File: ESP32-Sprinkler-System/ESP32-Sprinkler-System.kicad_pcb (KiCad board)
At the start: 2 copper layers, 207 x 158.8 mm, 58 parts, among them J101 12V, J102 DHT, J103 NEOPIXEL, J104 LCD, J105 BME280, J201 TBL004-508-02BE-2GY, J202 TBL004-508-02BE-2GY, J203 TBL004-508-02BE-2GY, J204 TBL004-508-02BE-2GY, Q201 IRFZ24NPBF, Q202 IRFZ24NPBF, Q203 IRFZ24NPBF, Q204 IRFZ24NPBF, U101 V7805-500, U102 ESP32-DEVKITC-32D, U201 MC33152PG, U202 MC33152PG

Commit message: Traces complete
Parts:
- moved S101 1.42 mm to (180.3, 120.7)
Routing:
- net 3.3V: track 0.00 -> 95.0 mm, vias 0 -> 2
- net SW_A: track 0.00 -> 73.2 mm
- net DHT: track 0.00 -> 65.7 mm, vias 0 -> 2
- net MOSI: track 0.00 -> 49.3 mm
- net SCK: track 0.00 -> 45.3 mm
- net D/C: track 0.00 -> 34.0 mm
- net 5V: track 30.7 -> 64.2 mm
- net BACKLIGHT: track 0.00 -> 26.3 mm
- net SDA: track 0.00 -> 24.9 mm
- net CS: track 0.00 -> 21.2 mm
- net 12V: track 241.9 -> 262.9 mm
- net SCL: track 0.00 -> 17.7 mm
- net NEOPIXEL: track 0.00 -> 16.7 mm
- net Valve1: track 0.00 -> 13.3 mm
- net Valve4: track 0.00 -> 9.91 mm
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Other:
- board size 207 x 158.8 mm -> 134.6 x 73.7 mm

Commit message: curvy 2 saved
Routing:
- net 12V: track 262.9 -> 257.8 mm
- net D/C: track 34.0 -> 33.0 mm
- net MOSI: track 49.3 -> 48.4 mm
- net SW_A: track 73.2 -> 72.3 mm
- net 3.3V: track 95.0 -> 94.2 mm
- net Net-(R218-Pad1): track 35.9 -> 35.1 mm
- net SCK: track 45.3 -> 44.6 mm
- net 5V: track 64.2 -> 63.5 mm
- net DHT: track 65.7 -> 65.1 mm
- net Net-(D206-Pad2): track 25.9 -> 25.3 mm
- net Net-(R202-Pad1): track 25.0 -> 24.4 mm

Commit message: added some labels and stuff
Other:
- board text added: "+12"
- board text added: "3.3V CS SCK MOSI DC BL GND"
- board text added: "3.3V GND SCL SDA"
- board text added: "3.3V IO5 GND"
- board text added: "5V IO2 GND"
- board text added: "GND"
- board text added: "IO23"
- board text added: "Power In"
- board text added: "Zone1:IO32"
- board text added: "Zone2:IO33"
- board text added: "Zone3:IO25"
- board text added: "Zone4:IO26"
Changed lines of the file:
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@@
     (property "Sheetname" "")
     (attr through_hole)
-    (fp_text reference "J105" (at 2.515 -0.02 180) (layer "F.SilkS")
-      (effects (font (size 1 1) (thickness 0.15)))
-    )
-    (fp_text value "BME280" (at 2.605 8.01 180) (layer "F.SilkS")
+    (fp_text reference "J105" (at 2.515 -0.02 180) (layer "F.SilkS") hide
+      (effects (font (size 1 1) (thickness 0.15)))
+    )
+    (fp_text value "BME280" (at 7.685 8.01 180) (layer "F.SilkS")
       (effects (font (size 1 1) (thickness 0.15)))
     )
@@
     (property "Sheetname" "")
     (attr exclude_from_pos_files)
-    (fp_text reference "S101" (at 0 -6.604) (layer "F.SilkS")
+    (fp_text reference "S101" (at 0 0) (layer "F.SilkS")
       (effects (font (size 0.6096 0.6096) (thickness 0.127)))
     )
@@
     (property "Sheetname" "")
     (attr through_hole)
-    (fp_text reference "J104" (at 2.3107 0.014 180) (layer "F.SilkS")
-      (effects (font (size 1 1) (thickness 0.15)))
-    )
-    (fp_text value "LCD" (at 2.4007 8.044 180) (layer "F.SilkS")
+    (fp_text reference "J104" (at 2.3107 0.014 180) (layer "F.SilkS") hide
+      (effects (font (size 1 1) (thickness 0.15)))
+    )
+    (fp_text value "LCD" (at 11.9257 7.409 180) (layer "F.SilkS")
       (effects (font (size 1 1) (thickness 0.15)))
     )
@@
     (property "Sheetname" "")
     (attr through_hole)
-    (fp_text reference "J102" (at 2.54 0 180) (layer "F.SilkS")
-      (effects (font (size 1 1) (thickness 0.15)))
-    )
-    (fp_text value "DHT" (at 2.63 4.22 180) (layer "F.SilkS")
+    (fp_text reference "J102" (at 2.54 0 180) (layer "F.SilkS") hide
+      (effects (font (size 1 1) (thickness 0.15)))
+    )
+    (fp_text value "DHT" (at -2.45 4.22 180) (layer "F.SilkS")
       (effects (font (size 1 1) (thickness 0.15)))
     )
@@
     (property "Sheetname" "")
     (attr through_hole)
-    (fp_text reference "U102" (at -10.829175 -24.765) (layer "F.SilkS")
+    (fp_text reference "U102" (at -10.829175 -24.765) (layer "F.SilkS") hide
       (effects (font (size 1.000386 1.000386) (thickness 0.15)))
     )
@@
     (property "Sheetname" "")
     (attr through_hole)
-    (fp_text reference "C105" (at 6.35 0 180) (layer "F.SilkS")
+    (fp_text reference "C105" (at 5.805 0 180) (layer "F.SilkS")
       (effects (font (size 1 1) (thickness 0.15)))
     )
@@
     (property "Sheetname" "")
     (attr through_hole)
-    (fp_text reference "J103" (at 2.54 0 180) (layer "F.SilkS")
-      (effects (font (size 1 1) (thickness 0.15)))
-    )
-    (fp_text value "NEOPIXEL" (at -2.45 2.54 180) (layer "F.SilkS")
+    (fp_text reference "J103" (at 2.54 0 180) (layer "F.SilkS") hide
+      (effects (font (size 1 1) (thickness 0.15)))
+    )
+    (fp_text value "NEOPIXEL" (at 7.075 2.54 180) (layer "F.SilkS")
       (effects (font (size 1 1) (thickness 0.15)))
     )
@@
   (gr_rect (start 355.28 125.1) (end 300.78 55.1) (layer "Dwgs.User") (width 0.15) (fill none))
   (gr_rect (start 58.01 61.05) (end 192.63 134.71) (layer "Edge.Cuts") (width 0.1) (fill none))
+  (gr_text "Power In" (at 109.22 133.985) (layer "F.SilkS")
+    (effects (font (size 1 1) (thickness 0.15)))
+  )
+  (gr_text "+12" (at 100.33 132.08) (layer "F.SilkS")
+    (effects (font (size 1 1) (thickness 0.15)))
+  )
+  (gr_text "+12" (at 60.96 97.79) (layer "F.SilkS")
+    (effects (font (size 1 1) (thickness 0.15)))
+  )
+  (gr_text "+12" (at 60.96 115.57) (layer "F.SilkS")
+    (effects (font (size 1 1) (thickness 0.15)))
+  )
+  (gr_text "GND" (at 116.84 132.08) (layer "F.SilkS")
+    (effects (font (size 1 1) (thickness 0.15)))
+  )
+  (gr_text "Zone2:IO33" (at 66.04 95.25) (layer "F.SilkS")
+    (effects (font (size 1 1) (thickness 0.15)))
+  )
+  (gr_text "3.3V\n\nGND\nSCL\n\nSDA" (at 172.308348 82.021383 90) (layer "F.SilkS")
+    (effects (font (size 1.5 1) (thickness 0.15)) (justify left))
+  )
+  (gr_text "Zone3:IO25" (at 66.04 113.03) (layer "F.SilkS")
+    (effects (font (size 1 1) (thickness 0.15)))
+  )
+  (gr_text "3.3V\nIO5\n\nGND" (at 107.315 67.945 90) (layer "F.SilkS")
+    (effects (font (size 1.5 1) (thickness 0.15)) (justify left))
+  )
+  (gr_text "IO23" (at 180.34 118.11) (layer "F.SilkS")
+    (effects (font (size 1 1) (thickness 0.15)))
+  )
+  (gr_text "+12" (at 60.96 80.01) (layer "F.SilkS")
+    (effects (font (size 1 1) (thickness 0.15)))
+  )
+  (gr_text "+12" (at 60.96 62.23) (layer "F.SilkS")
+    (effects (font (size 1 1) (thickness 0.15)))
+  )
+  (gr_text "3.3V\nCS\nSCK\nMOSI\nDC\nBL\nGND" (at 174.74745 107.95 90) (layer "F.SilkS")
+    (effects (font (size 1.5 1) (thickness 0.15)) (justify left))
+  )
+  (gr_text "Zone4:IO26" (at 66.04 130.81) (layer "F.SilkS")
+    (effects (font (size 1 1) (thickness 0.15)))
+  )
+  (gr_text "5V\nIO2\nGND" (at 166.034612 123.19 90) (layer "F.SilkS")
+    (effects (font (size 1.5 1) (thickness 0.15)) (justify left))
+  )
+  (gr_text "Zone1:IO32" (at 66.04 77.47) (layer "F.SilkS")
+    (effects (font (size 1 1) (thickness 0.15)))
+  )
   (dimension (type aligned) (layer "Dwgs.User")
     (pts (xy 355.28 36.6) (xy 300.78 36.6))

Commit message: TIDY UP AND ANOTATE
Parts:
- added REF**: Breadstick B Silk 5mm, _Breadstick_Footprints:Breadstick B Silk 5mm, F.Cu at (188.0, 130.8)
- added REF**: Breadstick B 10mm v2, _Breadstick_Footprints:Breadstick B 10mm v2, F.Cu at (174.6, 93.3)
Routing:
- net 3.3V: track 94.2 -> 108.3 mm, vias 2 -> 0
- net GND: track 7.83 -> 0.00 mm, vias 4 -> 0
- net D/C: track 33.0 -> 26.4 mm
- net CS: track 20.8 -> 22.9 mm
- net BACKLIGHT: track 25.9 -> 27.7 mm
- net 12V: track 257.8 -> 259.4 mm
- net Net-(R202-Pad1): track 24.4 -> 25.9 mm
- net MOSI: track 48.4 -> 49.7 mm
- net SCK: track 44.6 -> 45.3 mm
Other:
- board text added: "J & R Creative Technologies Inc."
- board text added: "https://github.com/mrangen/ESP32-Sprinkler-System"

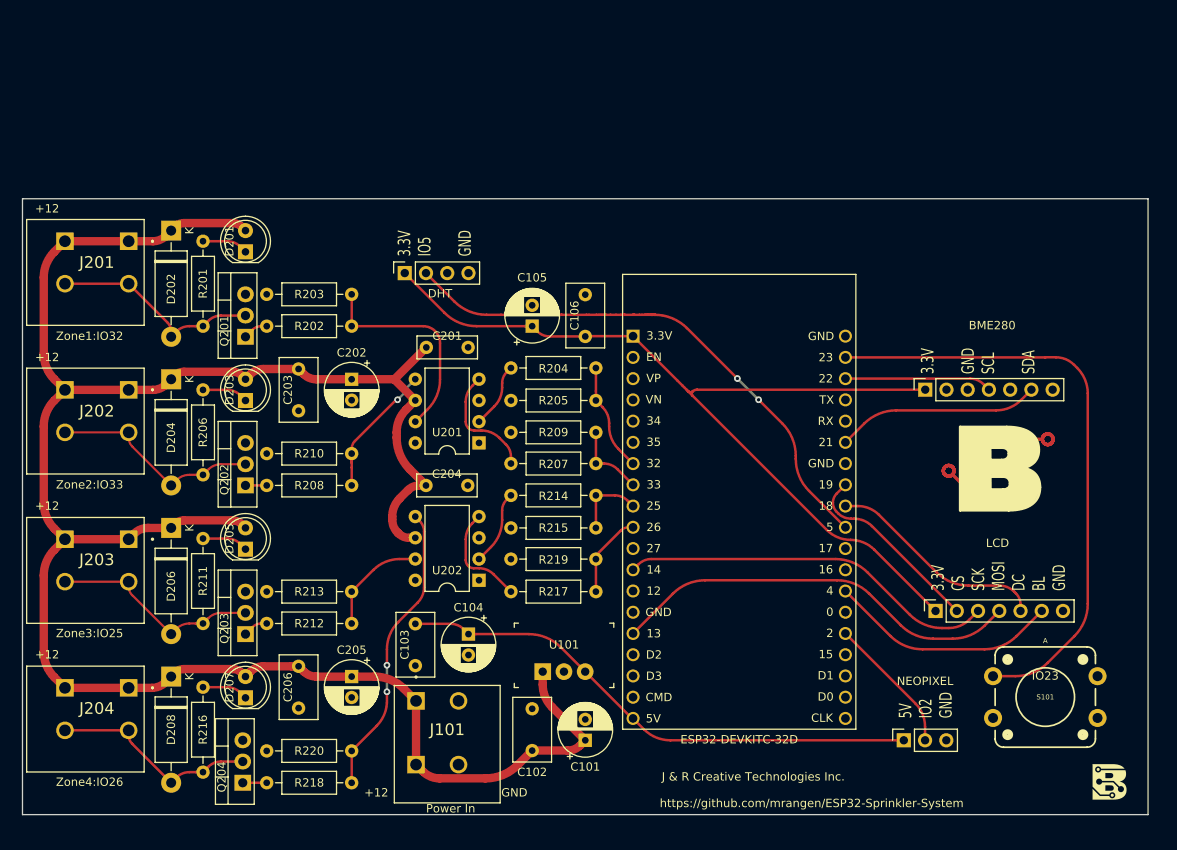
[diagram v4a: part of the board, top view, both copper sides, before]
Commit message: Added M3 Mounting Holes
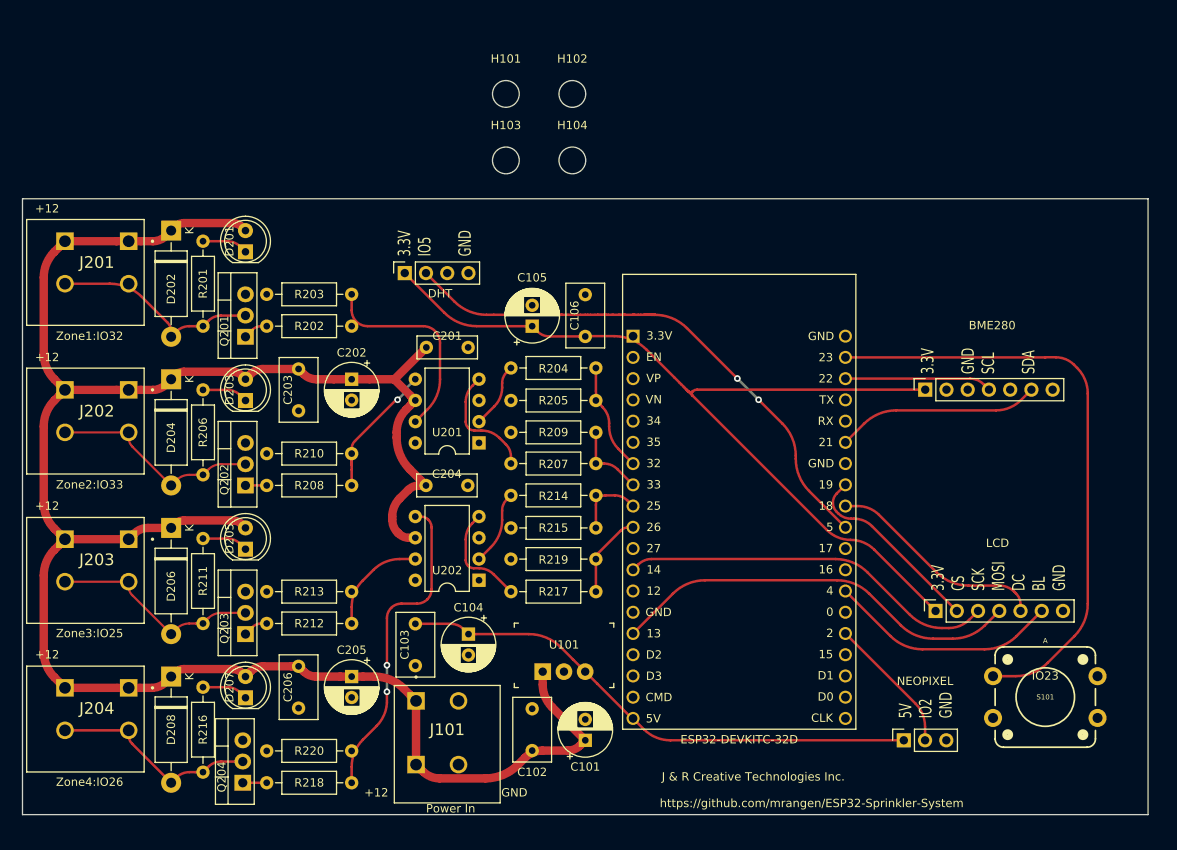
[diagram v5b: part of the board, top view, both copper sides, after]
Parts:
- removed REF**: Breadstick B Silk 5mm, _Breadstick_Footprints:Breadstick B Silk 5mm
- removed REF**: Breadstick B 10mm v2, _Breadstick_Footprints:Breadstick B 10mm v2
- added H101: MountingHole, MountingHole:MountingHole_3.2mm_M3, F.Cu at (115.8, 48.5)
- added H102: MountingHole, MountingHole:MountingHole_3.2mm_M3, F.Cu at (123.8, 48.5)
- added H103: MountingHole, MountingHole:MountingHole_3.2mm_M3, F.Cu at (115.8, 56.5)
- added H104: MountingHole, MountingHole:MountingHole_3.2mm_M3, F.Cu at (123.8, 56.5)
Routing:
- net 12V: track 259.4 -> 262.6 mm
- net Net-(R218-Pad1): track 35.2 -> 38.4 mm
- net Net-(R202-Pad1): track 25.9 -> 25.0 mm
- net Valve3: track 8.76 -> 8.23 mm

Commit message: Update ESP32-Sprinkler-System.kicad_pcb
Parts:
- moved H104 102.9 mm to (189.0, 136.0)
- moved H103 96.0 mm to (62.0, 136.0)
- moved H102 65.8 mm to (189.0, 57.0)
- moved H101 54.5 mm to (62.0, 57.0)
- moved J105 3.81 mm to (167.2, 80.3)
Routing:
- net SW_A: track 72.3 -> 0.00 mm
- net 3.3V: track 108.0 -> 80.8 mm
- net SDA: track 24.4 -> 0.00 mm
- net SCL: track 17.6 -> 0.00 mm
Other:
- board size 134.6 x 73.7 mm -> 135 x 87 mm
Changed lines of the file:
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@@
   )
   (footprint "Connector_PinSocket_2.54mm:PinSocket_1x07_P2.54mm_Vertical" (layer "F.Cu")
-    (at 165.98 83.885 90)
+    (at 167.1562 80.2632 90)
     (descr "Through hole straight socket strip, 1x07, 2.54mm pitch, single row (from Kicad 4.0.7), script generated")
     (tags "Through hole socket strip THT 1x07 2.54mm single row")
@@
   )
   (footprint "MountingHole:MountingHole_3.2mm_M3" (layer "F.Cu")
-    (at 123.774 48.514)
+    (at 189 57)
     (descr "Mounting Hole 3.2mm, no annular, M3")
     (tags "mounting hole 3.2mm no annular m3")
@@
   )
   (footprint "MountingHole:MountingHole_3.2mm_M3" (layer "F.Cu")
-    (at 115.824 56.464)
+    (at 62 136)
     (descr "Mounting Hole 3.2mm, no annular, M3")
     (tags "mounting hole 3.2mm no annular m3")
@@
   )
   (footprint "MountingHole:MountingHole_3.2mm_M3" (layer "F.Cu")
-    (at 115.824 48.514)
+    (at 62 57)
     (descr "Mounting Hole 3.2mm, no annular, M3")
     (tags "mounting hole 3.2mm no annular m3")
@@
     (fp_line (start 0 -1.33) (end 1.33 -1.33) (layer "F.SilkS") (width 0.12))
     (fp_line (start 1.33 -1.33) (end 1.33 0) (layer "F.SilkS") (width 0.12))
-    (fp_rect (start -2.3876 22.5438) (end 23.6124 -7.4562) (layer "Dwgs.User") (width 0.05) (fill none))
+    (fp_rect (start -1.5 22.5438) (end 24.5 -7.4562) (layer "Dwgs.User") (width 0.05) (fill none))
     (fp_line (start -1.8 17) (end -1.8 -1.8) (layer "F.CrtYd") (width 0.05))
     (fp_line (start -1.8 -1.8) (end 1.75 -1.8) (layer "F.CrtYd") (width 0.05))
@@
       (net 55 "unconnected-(U102-Pad38)") (pinfunction "CLK") (pintype "input"))
     (model "${KIPRJMOD}/Snap EDA/ESP32-DEVKITC-32D/ESP32-DEVKITC-32D.step"
-      (offset (xyz 0 0 3.5))
+      (offset (xyz 0 -3.08 3.5))
       (scale (xyz 1 1 1))
       (rotate (xyz -90 0 0))
@@
   )
   (footprint "MountingHole:MountingHole_3.2mm_M3" (layer "F.Cu")
-    (at 123.774 56.464)
+    (at 189 136)
     (descr "Mounting Hole 3.2mm, no annular, M3")
     (tags "mounting hole 3.2mm no annular m3")
@@
   (gr_rect (start 355.28 36.6) (end 300.78 143.6) (layer "Dwgs.User") (width 0.1) (fill none))
   (gr_rect (start 355.28 125.1) (end 300.78 55.1) (layer "Dwgs.User") (width 0.15) (fill none))
-  (gr_rect (start 58.01 61.05) (end 192.63 134.71) (layer "Edge.Cuts") (width 0.1) (fill none))
+  (gr_arc (start 58 57) (mid 59.171573 54.171573) (end 62 53) (layer "Edge.Cuts") (width 0.2))
+  (gr_line (start 189 53) (end 62 53) (layer "Edge.Cuts") (width 0.2))
+  (gr_line (start 62 140) (end 189 140) (layer "Edge.Cuts") (width 0.2))
+  (gr_line (start 58 57) (end 58 136) (layer "Edge.Cuts") (width 0.2))
+  (gr_arc (start 193 136) (mid 191.828427 138.828427) (end 189 140) (layer "Edge.Cuts") (width 0.2))
+  (gr_line (start 193 136) (end 193 57) (layer "Edge.Cuts") (width 0.2))
+  (gr_arc (start 62 140) (mid 59.171573 138.828427) (end 58 136) (layer "Edge.Cuts") (width 0.2))
+  (gr_arc (start 189 53) (mid 191.828427 54.171573) (end 193 57) (layer "Edge.Cuts") (width 0.2))
   (gr_text "Power In" (at 109.22 133.985) (layer "F.SilkS")
     (effects (font (size 1 1) (thickness 0.15)))
@@
   (segment (start 82.511974 66.13) (end 79.6 66.13) (width 0.3) (layer "F.Cu") (net 3))
   (arc (start 82.511974 66.13) (mid 83.341641 66.295031) (end 84.045 66.765) (width 0.3) (layer "F.Cu") (net 3))
-  (segment (start 138.693804 83.885) (end 165.934038 83.885) (width 0.3) (layer "F.Cu") (net 4))
   (segment (start 137.355 83.805) (end 137.45 83.9) (width 0.3) (layer "F.Cu") (net 4))
   (segment (start 137.614375 84.064375) (end 137.635625 84.085625) (width 0.3) (layer "F.Cu") (net 4))
@@
   (arc (start 161.811207 113.341207) (mid 163.576572 114.520786) (end 165.658963 114.935) (width 0.3) (layer "F.Cu") (net 18))
   (arc (start 176.925492 113.341207) (mid 175.160126 114.520786) (end 173.077736 114.935) (width 0.3) (layer "F.Cu") (net 18))
-  (segment (start 172.94 83.225) (end 173.6 83.885) (width 0.3) (layer "F.Cu") (net 20))
-  (segment (start 171.346619 82.565) (end 156.435 82.565) (width 0.3) (layer "F.Cu") (net 20))
-  (arc (start 172.94 83.225) (mid 172.20895 82.736528) (end 171.346619 82.565) (width 0.3) (layer "F.Cu") (net 20))
-  (segment (start 158.666207 87.953792) (end 156.435 90.185) (width 0.3) (layer "F.Cu") (net 22))
-  (segment (start 174.45491 86.36) (end 162.513963 86.36) (width 0.3) (layer "F.Cu") (net 22))
-  (segment (start 177.4425 85.1225) (end 178.68 83.885) (width 0.3) (layer "F.Cu") (net 22))
-  (arc (start 158.666207 87.953792) (mid 160.431572 86.774213) (end 162.513963 86.36) (width 0.3) (layer "F.Cu") (net 22))
-  (arc (start 174.45491 86.36) (mid 176.071782 86.038384) (end 177.4425 85.1225) (width 0.3) (layer "F.Cu") (net 22))
   (segment (start 129.271382 90.961382) (end 131.035 92.725) (width 0.3) (layer "F.Cu") (net 24))
   (segment (start 126.59 84.058976) (end 126.59 81.29) (width 0.3) (layer "F.Cu") (net 24))
@@
   (arc (start 101.597637 121.331846) (mid 101.238582 122.832202) (end 100.366098 124.103901) (width 0.3) (layer "F.Cu") (net 33))
   (segment (start 101.6 120.015) (end 101.6 116.84) (width 0.3) (layer "B.Cu") (net 33))
-  (segment (start 185.42 84.346051) (end 185.42 109.506036) (width 0.3) (layer "F.Cu") (net 34))
-  (segment (start 181.61 80.01) (end 180.350606 80.01) (width 0.3) (layer "F.Cu") (net 34))
-  (segment (start 176.775396 118.15064) (end 174.0916 118.15064) (width 0.3) (layer "F.Cu") (net 34))
-  (segment (start 180.623152 116.556847) (end 183.826207 113.353792) (width 0.3) (layer "F.Cu") (net 34))
-  (segment (start 180.314393 80.025) (end 156.435 80.025) (width 0.3) (layer "F.Cu") (net 34))
-  (segment (start 183.778025 80.908025) (end 184.15 81.28) (width 0.3) (layer "F.Cu") (net 34))
-  (arc (start 180.3325 80.0175) (mid 180.324192 80.02305) (end 180.314393 80.025) (width 0.3) (layer "F.Cu") (net 34))
-  (arc (start 185.42 84.346051) (mid 185.089937 82.686716) (end 184.15 81.28) (width 0.3) (layer "F.Cu") (net 34))
-  (arc (start 185.42 109.506036) (mid 185.005786 111.588426) (end 183.826207 113.353792) (width 0.3) (layer "F.Cu") (net 34))
-  (arc (start 183.778025 80.908025) (mid 182.783326 80.243389) (end 181.61 80.01) (width 0.3) (layer "F.Cu") (net 34))
-  (arc (start 176.775396 118.15064) (mid 178.857786 117.736426) (end 180.623152 116.556847) (width 0.3) (layer "F.Cu") (net 34))
-  (arc (start 180.3325 80.0175) (mid 180.340807 80.011949) (end 180.350606 80.01) (width 0.3) (layer "F.Cu") (net 34))
   (segment (start 76.425 76.925) (end 76.014506 77.335493) (width 0.3) (layer "F.Cu") (net 58))
   (segment (start 81.768025 75.02) (end 84.68 75.02) (width 0.3) (layer "F.Cu") (net 58))
@@
     (polygon
       (pts
-        (xy 247.24 193.13)
-        (xy 36.42 190.59)
-        (xy 36.42 28.03)
-        (xy 247.24 28.03)
+        (xy 193 140)
+        (xy 58 140)
+        (xy 58 53)
+        (xy 132 53)
+        (xy 132 77)
+        (xy 156 77)
+        (xy 156 53)
+        (xy 193 53)
       )
     )
